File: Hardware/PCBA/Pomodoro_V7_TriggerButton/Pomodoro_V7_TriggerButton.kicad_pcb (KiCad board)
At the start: 2 copper layers, 14 x 16.5 mm, 2 parts, among them J1 Conn_01x02_Pin, SW1 SW_Push

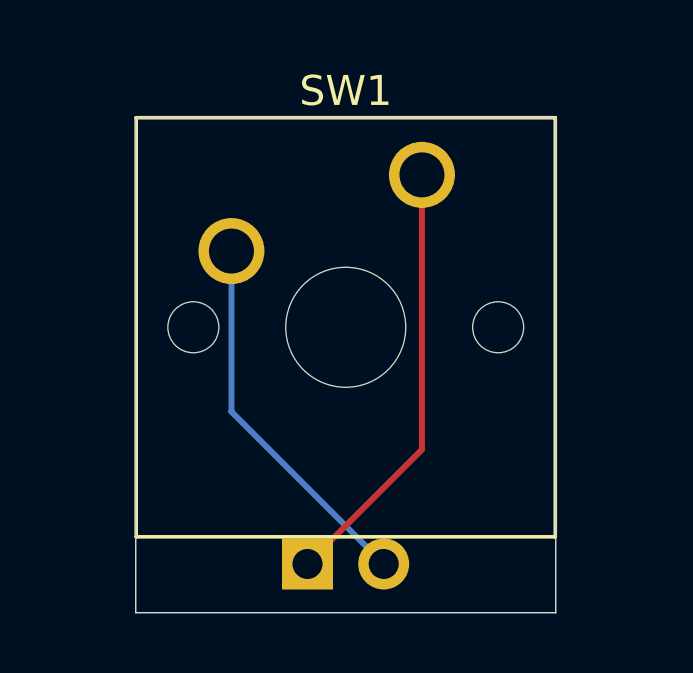
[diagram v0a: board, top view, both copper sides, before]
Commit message: added the selector wheel, changed the Connectors on the Trigger Button to move the assemlby closer together
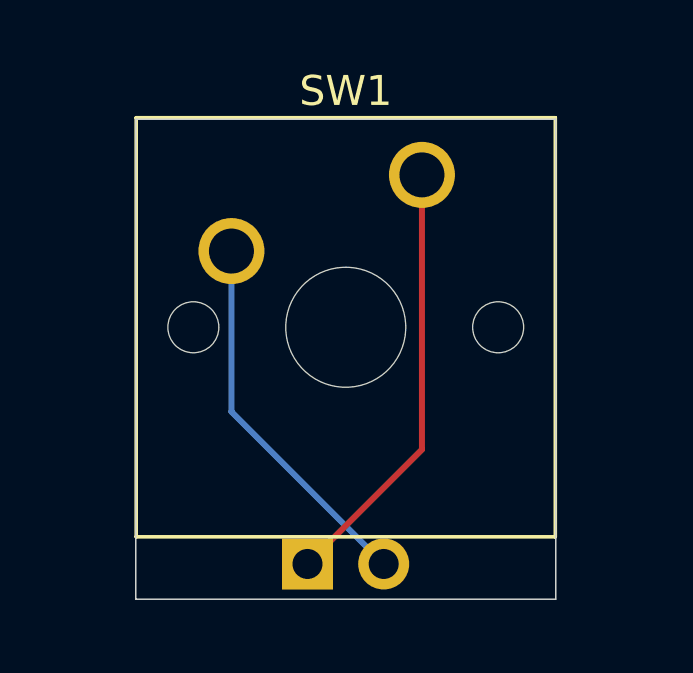
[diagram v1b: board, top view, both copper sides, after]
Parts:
- J1: value Conn_01x02_Pin -> Conn_01x02_Socket; footprint Connector_PinHeader_2.54mm:PinHeader_1x02_P2.54mm_Horizontal -> Connector_PinSocket_2.54mm:PinSocket_1x02_P2.54mm_Vertical
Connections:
- SW1 pad 1: Net-(J1-Pin_1) -> Net-(J1-Pin_2)
- SW1 pad 2: Net-(J1-Pin_2) -> Net-(J1-Pin_1)
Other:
- board size 14 x 16.5 mm -> 14 x 16 mm

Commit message: Increased the size for the Trigger Button PCB
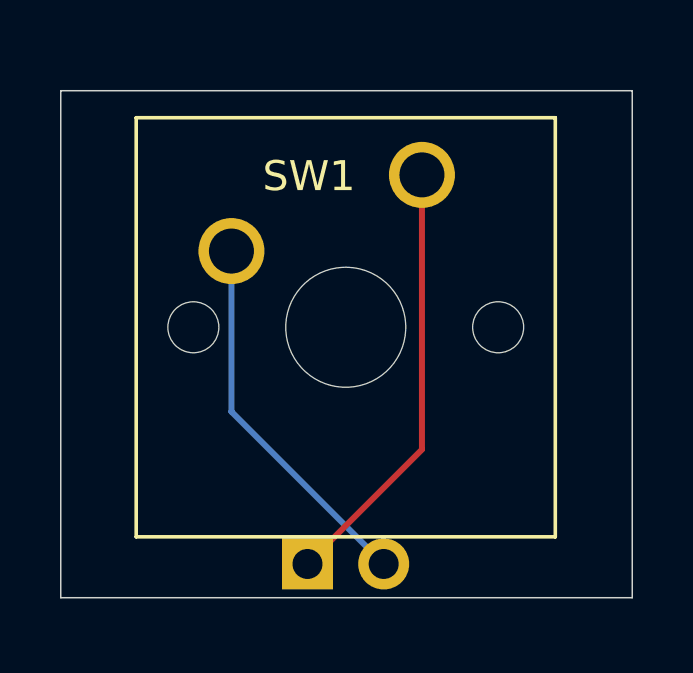
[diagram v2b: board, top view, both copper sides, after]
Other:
- board size 14 x 16 mm -> 19.1 x 16.9 mm
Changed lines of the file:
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@@
 		(tags "Cherry MX keyswitch 1.00u PCB")
 		(property "Reference" "SW1"
-			(at -2.54 -2.794 0)
+			(at -3.765 0.045 0)
 			(layer "F.SilkS")
 			(effects
@@
 	)
 	(gr_rect
-		(start 143 75.8)
-		(end 157 91.8)
+		(start 140.5 74.85)
+		(end 159.55 91.75)
 		(stroke
 			(width 0.05)
